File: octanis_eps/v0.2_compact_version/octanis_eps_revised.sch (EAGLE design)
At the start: 96 parts, among them IC1 OPA2333DGK, IC5 OPA2333DGK, IC7 OPA2333DGK, IC9 OPA2333DGK, Q1 FC-12M, Q2 N-HEXFET-2D_SOT232-, Q3 N-HEXFET-2D_SOT232-, Q4 N-HEXFET-2D_SOT232-

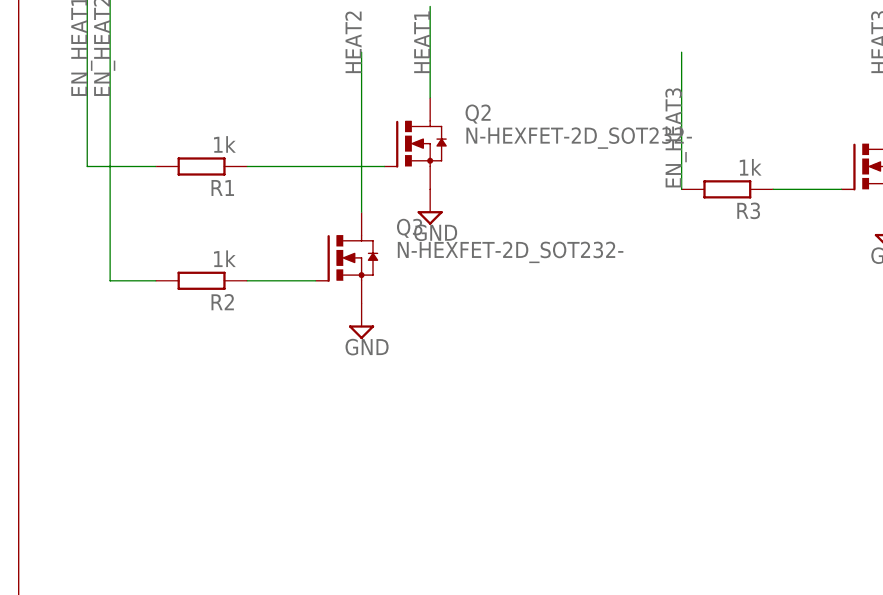
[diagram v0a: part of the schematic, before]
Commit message: added pull down on heat EN entries
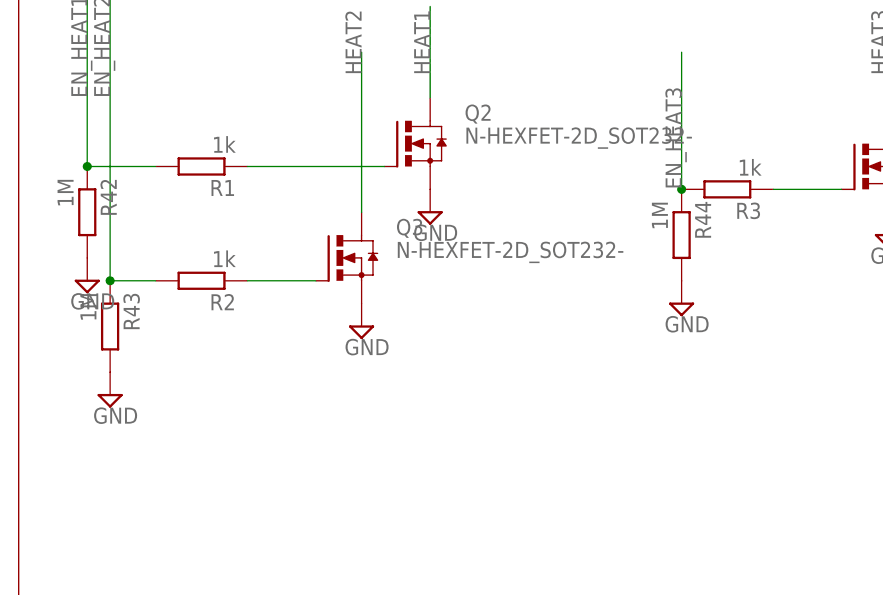
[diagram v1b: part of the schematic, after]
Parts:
- added R42, R43, R44: 1M, rcl:R-EU_R0603
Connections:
- net EN_HEAT1: now also R42.1
- net EN_HEAT2: now also R43.1
- net EN_HEAT3: now also R44.1
- net GND: now also R42.2, R43.2, R44.2
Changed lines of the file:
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@@
 <part name="VREF" library="pinhead" deviceset="PINHD-1X1" device=""/>
 <part name="VCC" library="pinhead" deviceset="PINHD-1X1" device=""/>
+<part name="R42" library="rcl" deviceset="R-EU_" device="R0603" value="1M"/>
+<part name="R43" library="rcl" deviceset="R-EU_" device="R0603" value="1M"/>
+<part name="R44" library="rcl" deviceset="R-EU_" device="R0603" value="1M"/>
+<part name="SUPPLY52" library="supply2" deviceset="GND" device=""/>
+<part name="SUPPLY53" library="supply2" deviceset="GND" device=""/>
+<part name="SUPPLY54" library="supply2" deviceset="GND" device=""/>
 </parts>
 <sheets>
@@
 <instance part="VREF" gate="G$1" x="439.42" y="-86.36"/>
 <instance part="VCC" gate="G$1" x="289.56" y="-12.7" rot="R270"/>
+<instance part="R42" gate="G$1" x="-33.02" y="58.42" rot="R270"/>
+<instance part="R43" gate="G$1" x="-30.48" y="45.72" rot="R270"/>
+<instance part="R44" gate="G$1" x="33.02" y="55.88" rot="R270"/>
+<instance part="SUPPLY52" gate="GND" x="-30.48" y="38.1"/>
+<instance part="SUPPLY53" gate="GND" x="33.02" y="48.26"/>
+<instance part="SUPPLY54" gate="GND" x="-33.02" y="50.8"/>
 </instances>
 <busses>
@@
 <pinref part="SUPPLY49" gate="GND" pin="GND"/>
 </segment>
+<segment>
+<pinref part="R43" gate="G$1" pin="2"/>
+<pinref part="SUPPLY52" gate="GND" pin="GND"/>
+</segment>
+<segment>
+<pinref part="R44" gate="G$1" pin="2"/>
+<pinref part="SUPPLY53" gate="GND" pin="GND"/>
+</segment>
+<segment>
+<pinref part="R42" gate="G$1" pin="2"/>
+<pinref part="SUPPLY54" gate="GND" pin="GND"/>
+</segment>
 </net>
 <net name="VCC" class="0">
@@
 <label x="-33.02" y="71.12" size="1.778" layer="95" rot="R90"/>
 <wire x1="-33.02" y1="63.5" x2="-33.02" y2="86.36" width="0.1524" layer="91"/>
+<pinref part="R42" gate="G$1" pin="1"/>
+<junction x="-33.02" y="63.5"/>
 </segment>
 <segment>
@@
 <label x="-30.48" y="71.12" size="1.778" layer="95" rot="R90"/>
 <wire x1="-30.48" y1="50.8" x2="-30.48" y2="86.36" width="0.1524" layer="91"/>
+<pinref part="R43" gate="G$1" pin="1"/>
+<junction x="-30.48" y="50.8"/>
 </segment>
 <segment>
@@
 <wire x1="33.02" y1="60.96" x2="33.02" y2="76.2" width="0.1524" layer="91"/>
 <label x="33.02" y="60.96" size="1.778" layer="95" rot="R90"/>
-</segment>
-<segment>
+<pinref part="R44" gate="G$1" pin="1"/>
+<junction x="33.02" y="60.96"/>
+</segment>
+<segment>

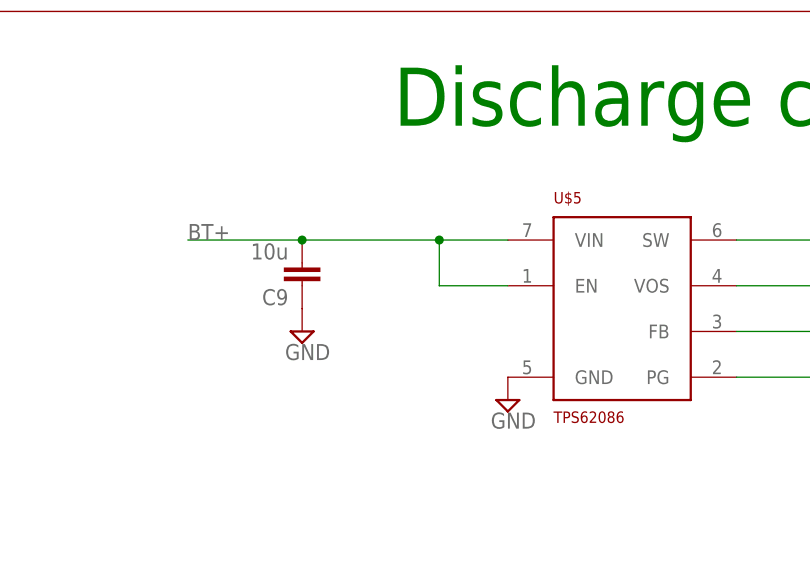
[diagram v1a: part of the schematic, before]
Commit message: added 0Ohm jumper on discharge circuit
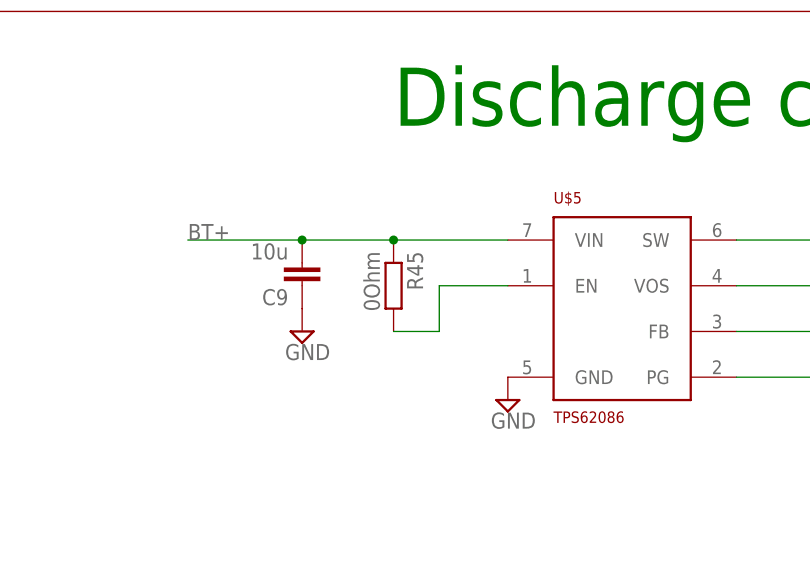
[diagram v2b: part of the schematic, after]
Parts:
- added R45: 0Ohm, rcl:R-EU_R0603
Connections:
- new net N$30: R45.2, U$5.EN
- net BT+: now also R45.1; no longer U$5.EN
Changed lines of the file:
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@@
 <part name="SUPPLY53" library="supply2" deviceset="GND" device=""/>
 <part name="SUPPLY54" library="supply2" deviceset="GND" device=""/>
+<part name="R45" library="rcl" deviceset="R-EU_" device="R0603" value="0Ohm"/>
 </parts>
 <sheets>
@@
 <instance part="SUPPLY53" gate="GND" x="33.02" y="48.26"/>
 <instance part="SUPPLY54" gate="GND" x="-33.02" y="50.8"/>
+<instance part="R45" gate="G$1" x="299.72" y="-167.64" rot="R270"/>
 </instances>
 <busses>
@@
 <pinref part="U$5" gate="G$1" pin="VIN"/>
 <pinref part="C9" gate="G$1" pin="2"/>
-<wire x1="312.42" y1="-162.56" x2="304.8" y2="-162.56" width="0.1524" layer="91"/>
-<wire x1="304.8" y1="-162.56" x2="289.56" y2="-162.56" width="0.1524" layer="91"/>
+<wire x1="312.42" y1="-162.56" x2="299.72" y2="-162.56" width="0.1524" layer="91"/>
+<wire x1="299.72" y1="-162.56" x2="289.56" y2="-162.56" width="0.1524" layer="91"/>
 <wire x1="289.56" y1="-162.56" x2="276.86" y2="-162.56" width="0.1524" layer="91"/>
 <junction x="289.56" y="-162.56"/>
 <label x="276.86" y="-162.56" size="1.778" layer="95"/>
-<pinref part="U$5" gate="G$1" pin="EN"/>
-<wire x1="312.42" y1="-167.64" x2="304.8" y2="-167.64" width="0.1524" layer="91"/>
-<wire x1="304.8" y1="-167.64" x2="304.8" y2="-162.56" width="0.1524" layer="91"/>
-<junction x="304.8" y="-162.56"/>
+<pinref part="R45" gate="G$1" pin="1"/>
+<junction x="299.72" y="-162.56"/>
 </segment>
 <segment>
@@
 </segment>
 </net>
+<net name="N$30" class="0">
+<segment>
+<pinref part="U$5" gate="G$1" pin="EN"/>
+<wire x1="312.42" y1="-167.64" x2="304.8" y2="-167.64" width="0.1524" layer="91"/>
+<pinref part="R45" gate="G$1" pin="2"/>
+<wire x1="299.72" y1="-172.72" x2="304.8" y2="-172.72" width="0.1524" layer="91"/>
+<wire x1="304.8" y1="-172.72" x2="304.8" y2="-167.64" width="0.1524" layer="91"/>
+</segment>
+</net>
